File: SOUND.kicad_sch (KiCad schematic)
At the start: 12 parts, among them Y1 14.318Mhz

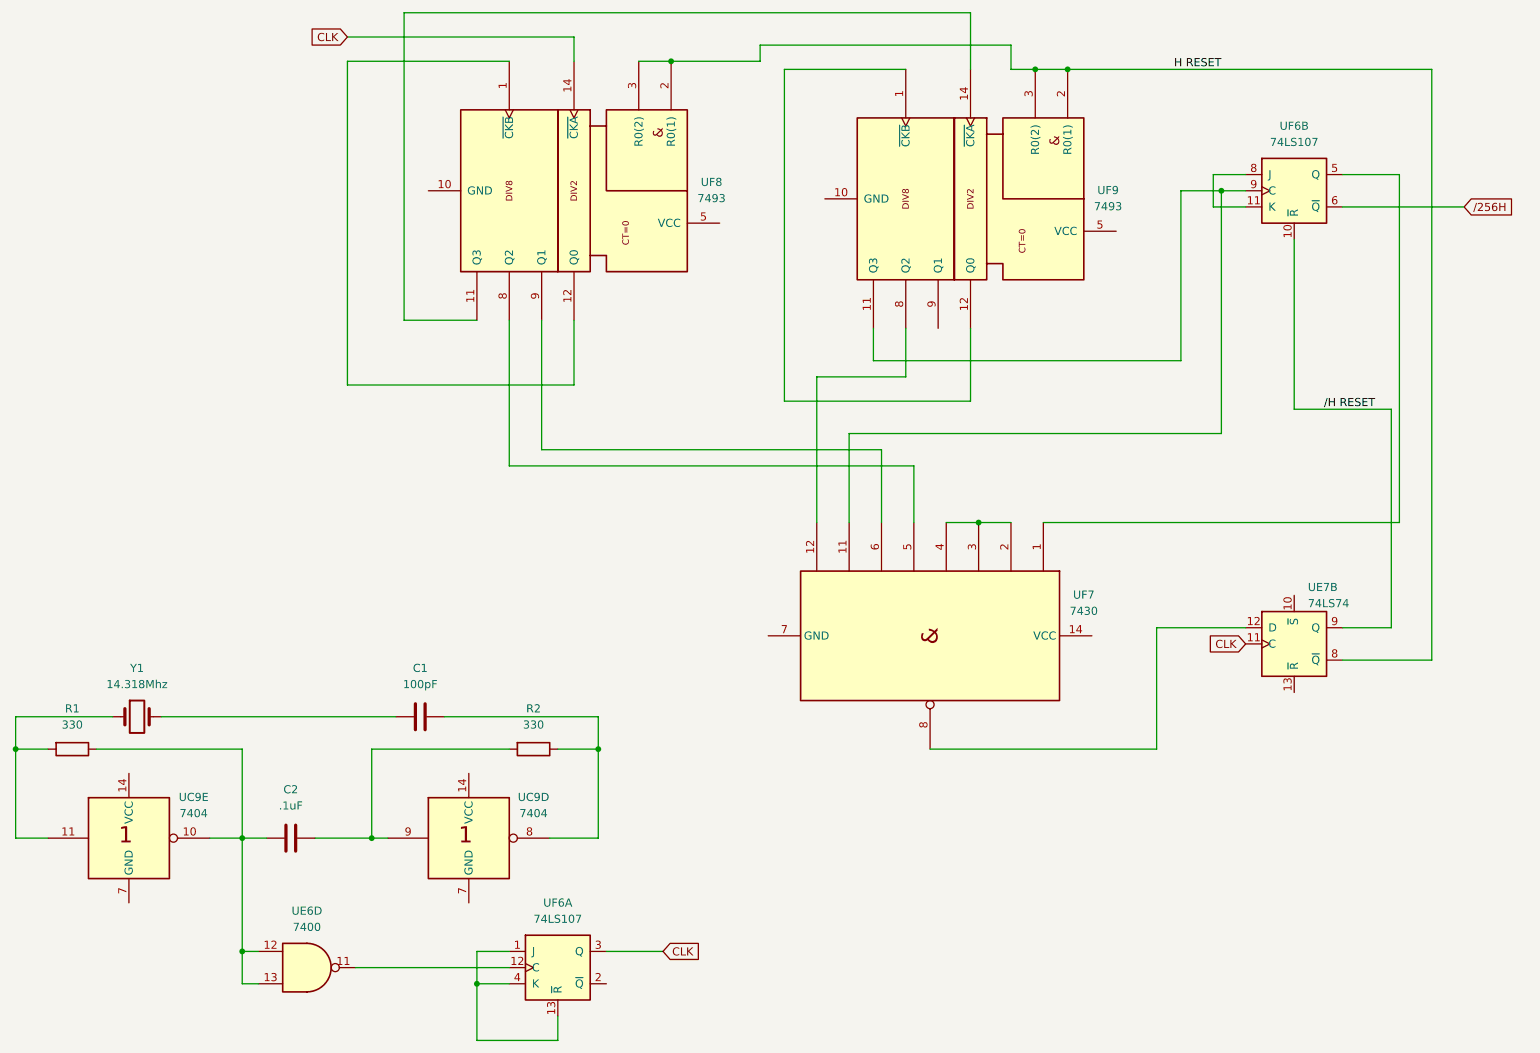
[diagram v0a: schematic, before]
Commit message: Added remainder of sheets
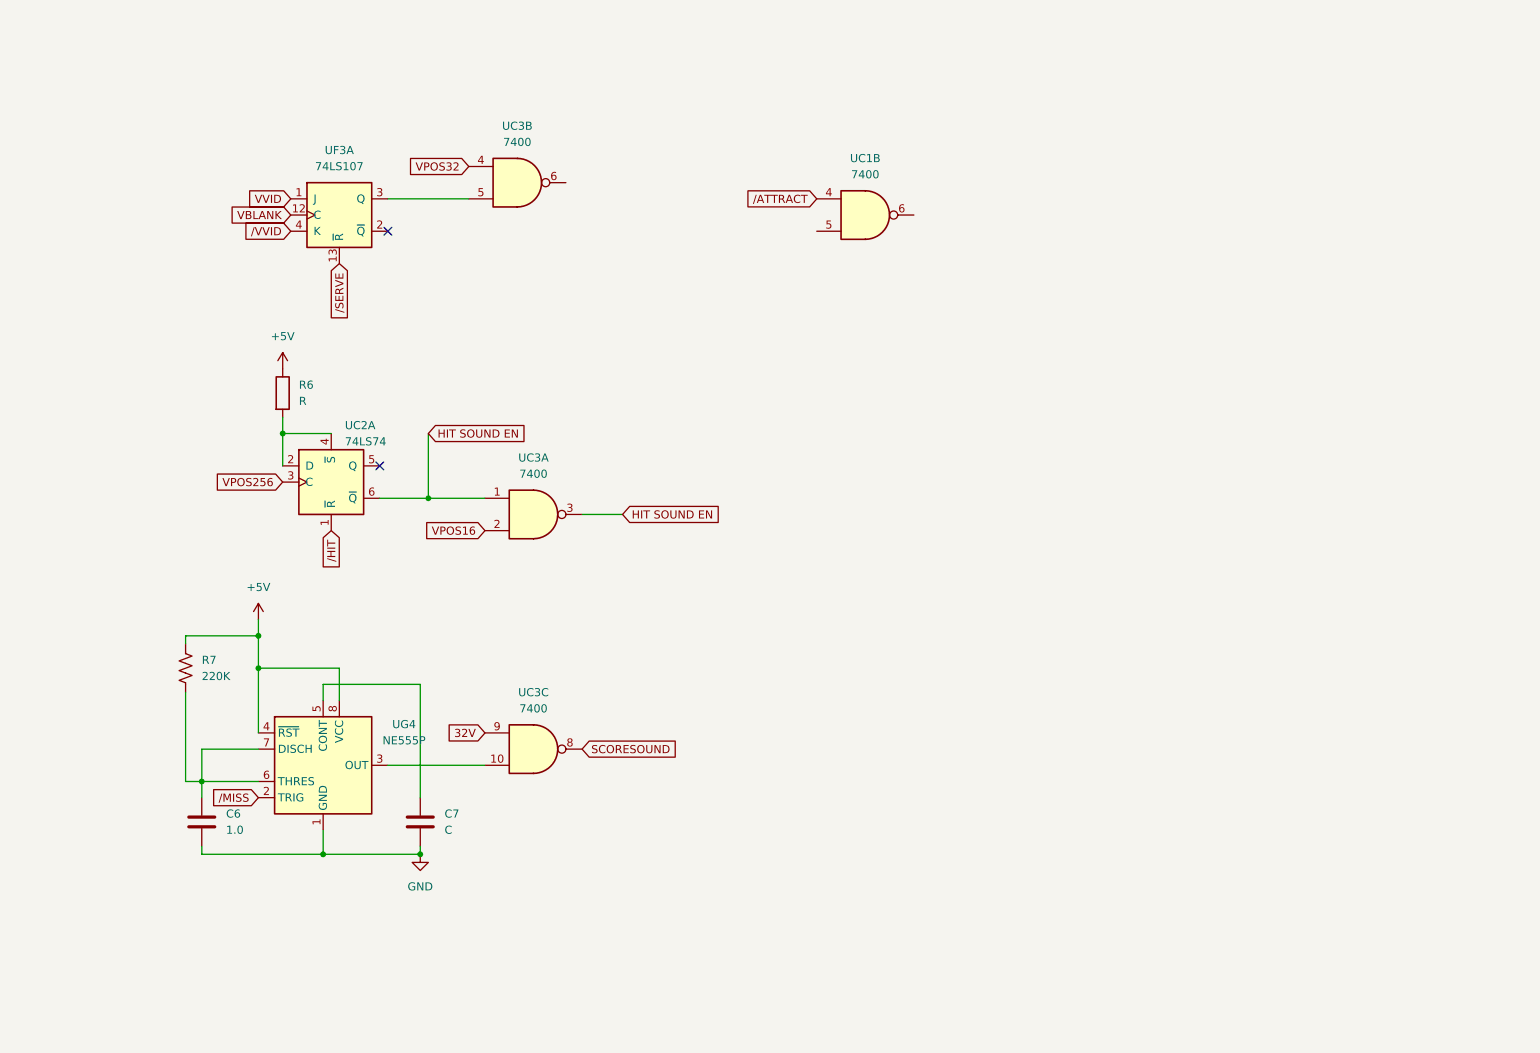
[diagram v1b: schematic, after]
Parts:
- removed C1: 100pF, symbol Device:C
- removed C2: .1uF, symbol Device:C
- removed R1, R2: 330, symbol Device:R
- removed UC9: 7404, Package_DIP:DIP-14_W7.62mm_Socket_LongPads, symbol 74xx_IEEE:7404
- removed UE6: 7400, Package_DIP:DIP-14_W7.62mm_Socket_LongPads, symbol 74xx:7400
- removed UE7: 74LS74, Package_DIP:DIP-14_W7.62mm_Socket_LongPads, symbol 74xx:74LS74
- removed UF6: 74LS107, Package_DIP:DIP-14_W7.62mm_Socket_LongPads, symbol 74xx:74LS107
- removed UF7: 7430, Package_DIP:DIP-14_W7.62mm_Socket_LongPads, symbol 74xx_IEEE:7430
- removed UF8, UF9: 7493, Package_DIP:DIP-14_W7.62mm_Socket_LongPads, symbol 74xx_IEEE:7493
- removed Y1: 14.318Mhz, symbol Device:Crystal
- added C6: 1.0, symbol Device:C
- added C7: C, symbol Device:C
- added R6: R, symbol Device:R
- added R7: 220K, symbol Device:R_US
- added UC1, UC3: 7400, Package_DIP:DIP-14_W7.62mm_Socket_LongPads, symbol 74xx:7400
- added UC2: 74LS74, Package_DIP:DIP-14_W7.62mm_Socket_LongPads, symbol 74xx:74LS74
- added UF3: 74LS107, Package_DIP:DIP-14_W7.62mm_Socket_LongPads, symbol 74xx:74LS107
- added UG4: NE555P, Package_DIP:DIP-8_W7.62mm_Socket_LongPads, symbol Timer:NE555P
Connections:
- new net: UC3.5, UF3.3 (Q)
- new net: UC3.10, UG4.3 (OUT)
- new net: C7.1, UG4.5 (CONT)
- new net: C6.1, R7.2, UG4.6 (THRES), UG4.7 (DISCH)
- new net: R6.2, UC2.2 (D), UC2.4 (~{S})
- new net +5V: R6.1, R7.1, UG4.4 (~{RST}), UG4.8 (VCC)
- new net 32V: UC3.9
- new net GND: C6.2, C7.2, UG4.1 (GND)
- new net HIT SOUND EN: UC2.6 (~{Q}), UC3.1, UC3.3
- new net SCORESOUND: UC3.8
- new net VBLANK: UF3.12 (C)
- new net VPOS16: UC3.2
- new net VPOS256: UC2.3 (C)
- new net VPOS32: UC3.4
- new net VVID: UF3.1 (J)
- new net /ATTRACT: UC1.4
- new net /HIT: UC2.1 (~{R})
- new net /MISS: UG4.2 (TRIG)
- new net /SERVE: UF3.13 (~{R})
- new net /VVID: UF3.4 (K)
- no-connect marks 0 -> 2

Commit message: R20260915
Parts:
- R6: value R -> R_US; symbol Device:R -> Device:R_US
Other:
- company: (none) -> Atari
- title: (none) -> PONG
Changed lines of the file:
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@@
 	(generator "eeschema")
 	(generator_version "10.0")
-	(paper "A4")
+	(paper "USLetter")
+	(title_block
+		(title "PONG")
+		(company "Atari")
+	)
 	(junction
 		(at 46.99 151.13)
@@
 	)
 	(symbol
-		(lib_id "Device:R")
+		(lib_id "Device:R_US")
 		(at 59.69 90.17 0)
 		(unit 1)
@@
 			)
 		)
-		(property "Value" "R"
+		(property "Value" "R_US"
 			(at 62.23 91.4399 0)
 			(show_name no)
@@
 		)
 		(property "Footprint" ""
-			(at 57.912 90.17 90)
+			(at 60.706 90.424 90)
 			(hide yes)
 			(show_name no)
@@
 			)
 		)
-		(property "Description" "Resistor"
+		(property "Description" "Resistor, US symbol"
 			(at 59.69 90.17 0)
 			(hide yes)

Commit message: R20260918
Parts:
- UC1, UC2, UC3, UF3: footprint Package_DIP:DIP-14_W7.62mm_Socket_LongPads -> pong:pong_DIP-14_W7.62mm_Socket_LongPads
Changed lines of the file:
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@@
 			)
 		)
-		(property "Footprint" "Package_DIP:DIP-14_W7.62mm_Socket_LongPads"
+		(property "Footprint" "pong:pong_DIP-14_W7.62mm_Socket_LongPads"
 			(at 96.52 57.15 0)
 			(hide yes)
@@
 			)
 		)
-		(property "Footprint" "Package_DIP:DIP-14_W7.62mm_Socket_LongPads"
+		(property "Footprint" "pong:pong_DIP-14_W7.62mm_Socket_LongPads"
 			(at 68.58 62.23 0)
 			(hide yes)
@@
 			)
 		)
-		(property "Footprint" "Package_DIP:DIP-14_W7.62mm_Socket_LongPads"
+		(property "Footprint" "pong:pong_DIP-14_W7.62mm_Socket_LongPads"
 			(at 151.13 62.23 0)
 			(hide yes)
@@
 			)
 		)
-		(property "Footprint" "Package_DIP:DIP-14_W7.62mm_Socket_LongPads"
+		(property "Footprint" "pong:pong_DIP-14_W7.62mm_Socket_LongPads"
 			(at 99.06 109.22 0)
 			(hide yes)
@@
 			)
 		)
-		(property "Footprint" "Package_DIP:DIP-14_W7.62mm_Socket_LongPads"
+		(property "Footprint" "pong:pong_DIP-14_W7.62mm_Socket_LongPads"
 			(at 67.31 104.14 0)
 			(hide yes)
@@
 			)
 		)
-		(property "Footprint" "Package_DIP:DIP-14_W7.62mm_Socket_LongPads"
+		(property "Footprint" "pong:pong_DIP-14_W7.62mm_Socket_LongPads"
 			(at 99.06 146.05 0)
 			(hide yes)

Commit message: R20260922
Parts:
- C7: footprint (none) -> Capacitor_THT:C_Disc_D16.0mm_W5.0mm_P10.00mm
- R6: value R_US -> R; footprint (none) -> Resistor_THT:R_Axial_DIN0207_L6.3mm_D2.5mm_P10.16mm_Horizontal
- R7: footprint (none) -> Resistor_THT:R_Axial_DIN0207_L6.3mm_D2.5mm_P10.16mm_Horizontal
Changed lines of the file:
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@@
 			)
 		)
-		(property "Footprint" ""
+		(property "Footprint" "Capacitor_THT:C_Disc_D16.0mm_W5.0mm_P10.00mm"
 			(at 82.2452 161.29 0)
 			(hide yes)
@@
 			)
 		)
-		(property "Footprint" ""
+		(property "Footprint" "Resistor_THT:R_Axial_DIN0207_L6.3mm_D2.5mm_P10.16mm_Horizontal"
 			(at 45.466 133.604 90)
 			(hide yes)
@@
 			)
 		)
-		(property "Value" "R_US"
+		(property "Value" "R"
 			(at 62.23 91.4399 0)
 			(show_name no)
@@
 			)
 		)
-		(property "Footprint" ""
+		(property "Footprint" "Resistor_THT:R_Axial_DIN0207_L6.3mm_D2.5mm_P10.16mm_Horizontal"
 			(at 60.706 90.424 90)
 			(hide yes)

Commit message: R20260922PM
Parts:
- C6: footprint (none) -> Capacitor_THT:C_Axial_L3.8mm_D2.6mm_P10.00mm_Horizontal
- C7: value C -> .1; footprint Capacitor_THT:C_Disc_D16.0mm_W5.0mm_P10.00mm -> Capacitor_THT:C_Axial_L3.8mm_D2.6mm_P10.00mm_Horizontal
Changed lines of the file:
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@@
 			)
 		)
-		(property "Value" "C"
+		(property "Value" ".1"
 			(at 85.09 158.7499 0)
 			(show_name no)
@@
 			)
 		)
-		(property "Footprint" "Capacitor_THT:C_Disc_D16.0mm_W5.0mm_P10.00mm"
+		(property "Footprint" "Capacitor_THT:C_Axial_L3.8mm_D2.6mm_P10.00mm_Horizontal"
 			(at 82.2452 161.29 0)
 			(hide yes)
@@
 			)
 		)
-		(property "Footprint" ""
+		(property "Footprint" "Capacitor_THT:C_Axial_L3.8mm_D2.6mm_P10.00mm_Horizontal"
 			(at 47.9552 161.29 0)
 			(hide yes)

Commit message: R20260924
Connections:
- net 16: now reaches UC1.6
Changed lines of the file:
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@@
+		)
+	)
+	(global_label "16"
+		(shape input)
+		(at 158.75 62.23 0)
+		(fields_autoplaced yes)
+		(effects
+			(font
+				(size 1.27 1.27)
+			)
+			(justify left)
+		)
+		(property "Intersheetrefs" "${INTERSHEET_REFS}"
+			(at 164.1542 62.23 0)
+			(hide yes)
+			(show_name no)
+			(do_not_autoplace no)
+			(effects
+				(font
+					(size 1.27 1.27)
+				)
+				(justify left)
+			)
 		)
 	)
